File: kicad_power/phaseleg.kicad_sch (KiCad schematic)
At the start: 14 parts, among them Q1 NMOS, Q2 NMOS

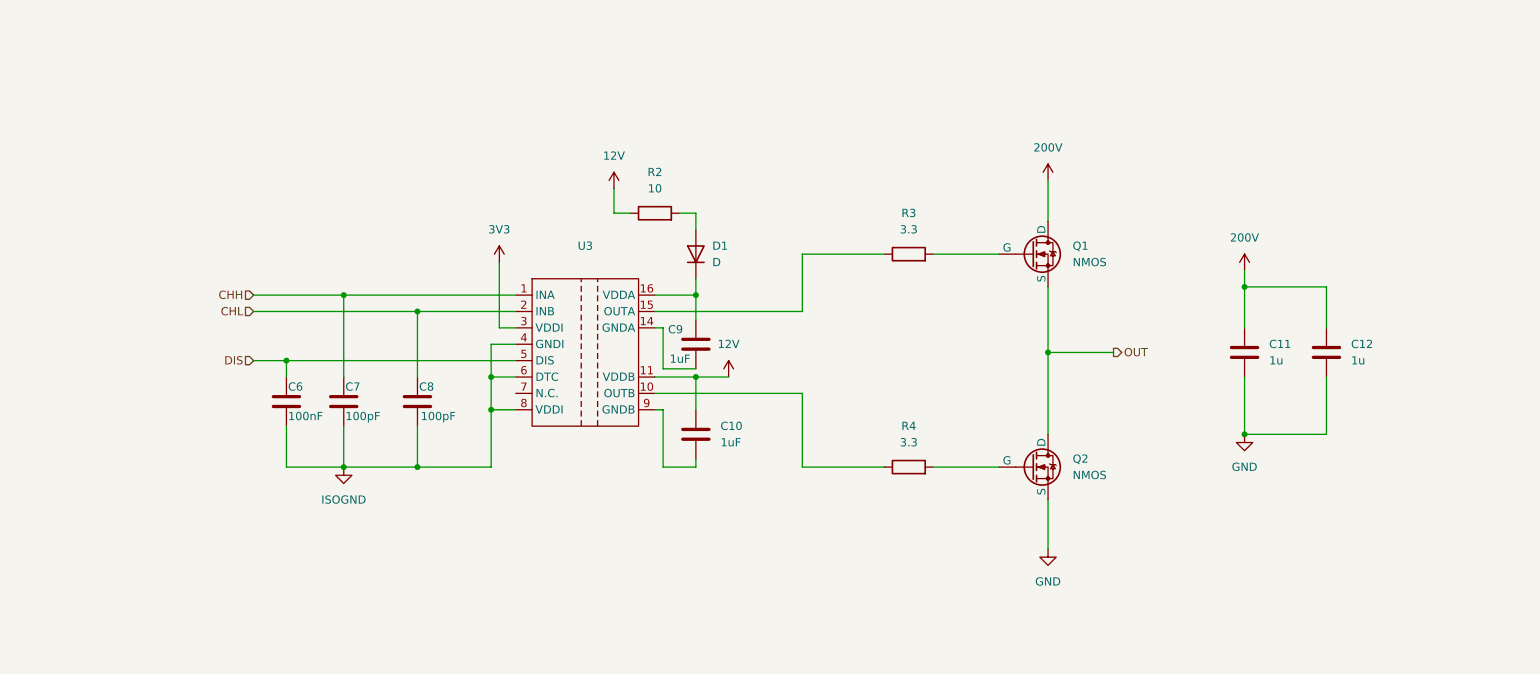
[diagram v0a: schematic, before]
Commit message: finished initial layout of power stage in KiCAD
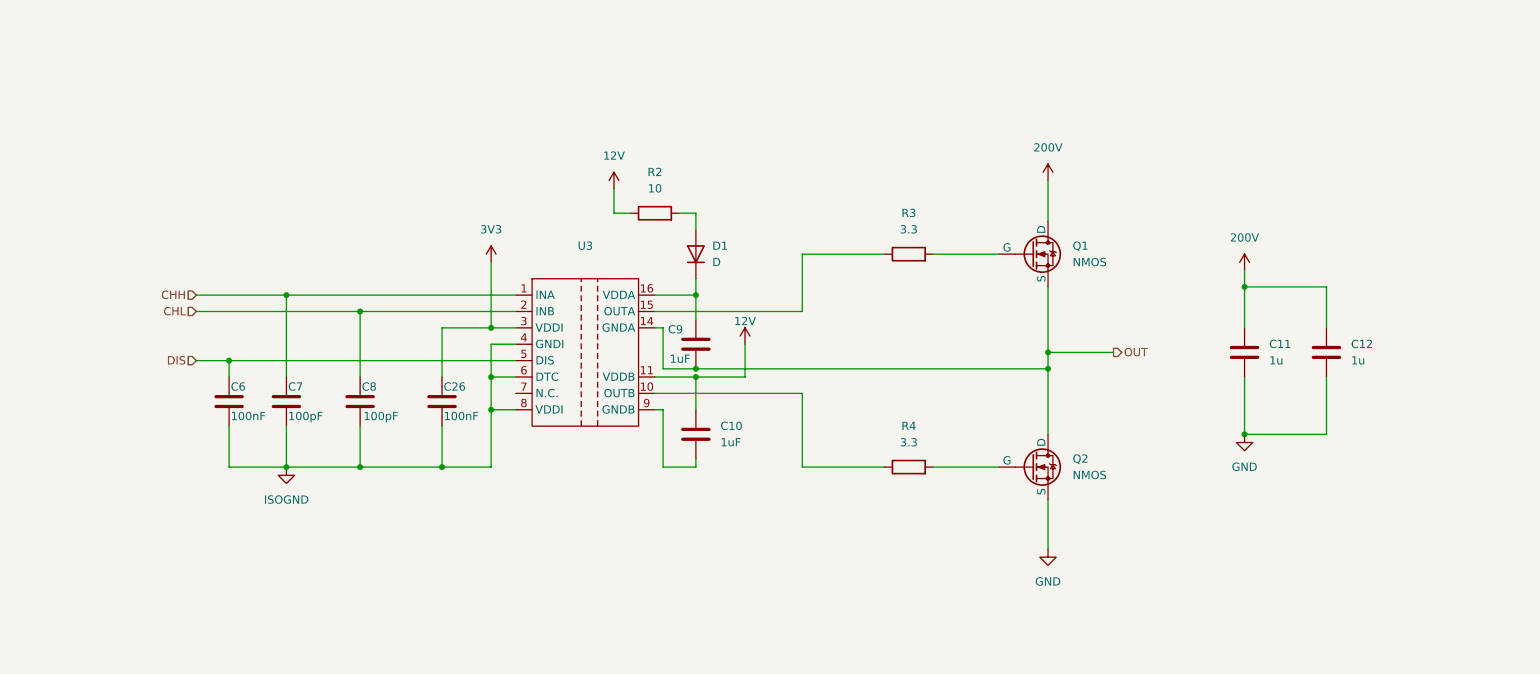
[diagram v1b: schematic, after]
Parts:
- added C26: 100nF, Capacitor_SMD:C_0402_1005Metric, symbol Device:C
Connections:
- net 3V3: now also C26.1
- net ISOGND: now also C26.2
- net OUT: now also C9.2, U3.14 (GNDA)
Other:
- moved on the sheet: C6, C7, C8

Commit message: adjustment to PCB layout, created BOM file, added MOSFET gate discharge diodes
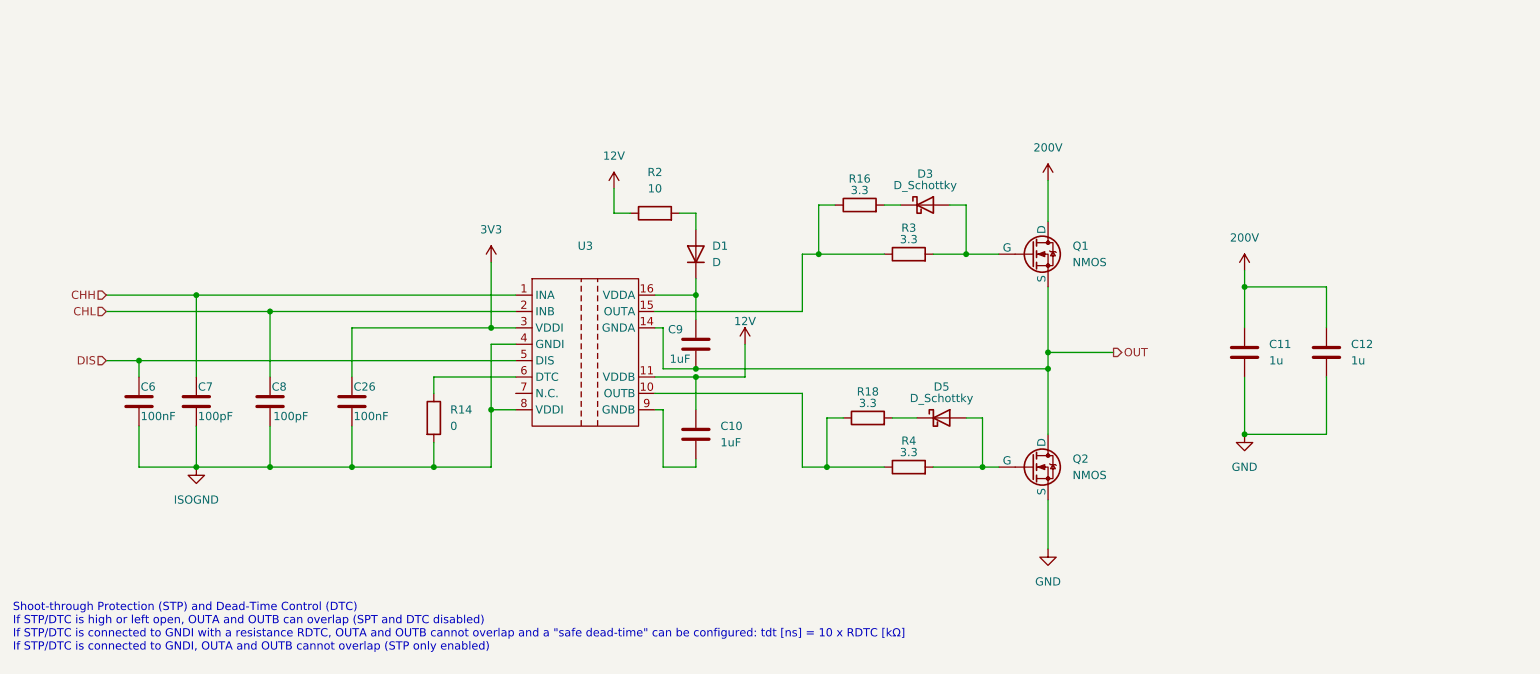
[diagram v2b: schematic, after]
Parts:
- added D3, D5: D_Schottky, Diode_SMD:D_SOD-323F, symbol Device:D_Schottky
- added R14: 0, Resistor_SMD:R_0402_1005Metric, symbol Device:R
- added R16, R18: 3.3, Resistor_SMD:R_0603_1608Metric, symbol Device:R
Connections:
- net ISOGND: now also R14.2; no longer U3.6 (DTC)
- net at Q2.1 (G), R4.2: now also D5.2 (A)
- net at R3.1, U3.15 (OUTA): now also R16.1
- net at Q1.1 (G), R3.2: now also D3.2 (A)
- net at R4.1, U3.10 (OUTB): now also R18.1
- new net: D5.1 (K), R18.2
- new net: R14.1, U3.6 (DTC)
- new net: D3.1 (K), R16.2
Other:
- note added: "Shoot-through Protection (STP) and Dead-Time Control (DTC) If STP/DTC is high or left open, OUTA and OUTB can overlap (SPT and DTC disabled) If STP/DTC is connected to GNDI with a resistance RDTC, OUTA and OUTB cannot overlap and a "safe dead-time" can be configured: tdt [ns] = 10 x RDTC [kΩ] If STP/DTC is connected to GNDI, OUTA and OUTB cannot overlap (STP only enabled)"
- moved on the sheet: C26, C6, C7, C8

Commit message: introduced AGND and A3V3, ensures HV design rules
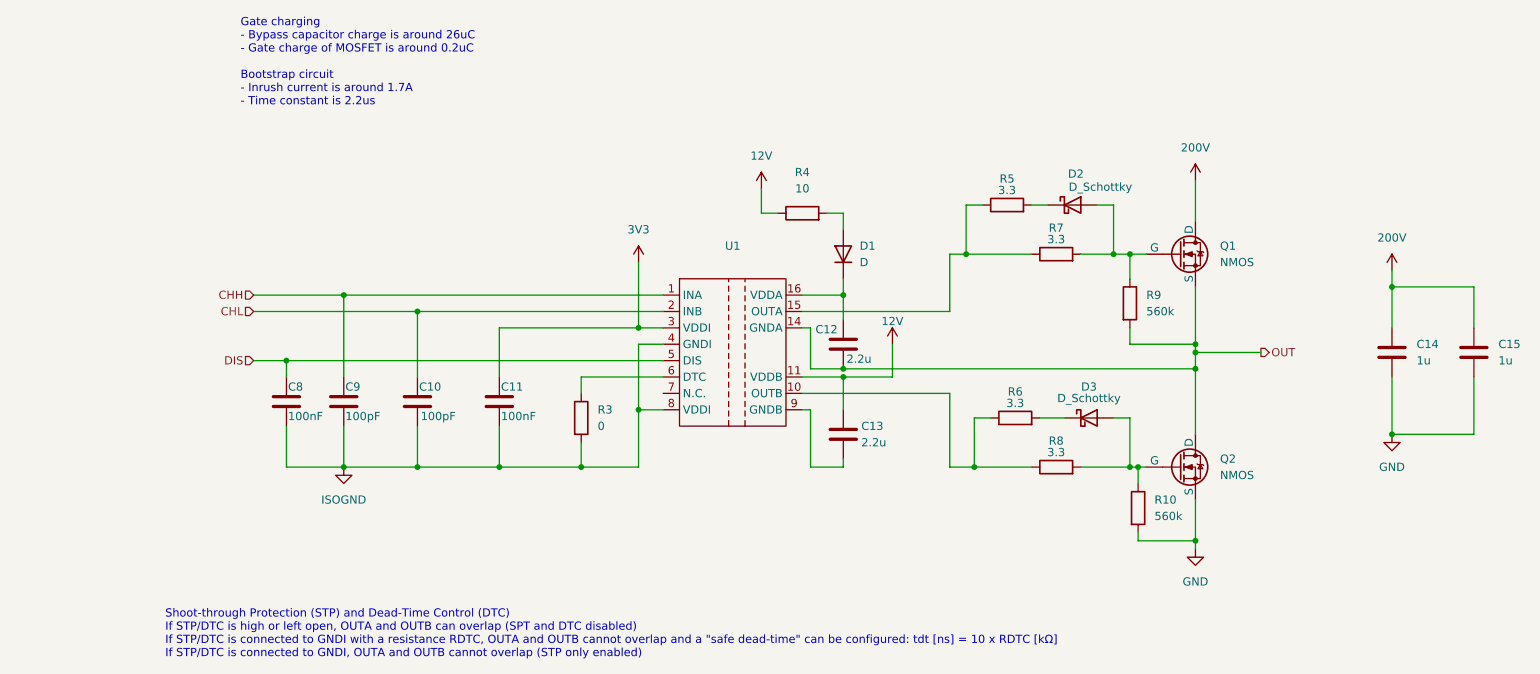
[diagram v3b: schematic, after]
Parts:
- added R10, R9: 560k, Resistor_SMD:R_0402_1005Metric, symbol Device:R
- C12: renamed from C9; value 1uF -> 2.2u; Partno C0603C105K3RACTU -> CGA3E1X7S1C225K080AE
- C13: renamed from C10; value 1uF -> 2.2u; Partno C0603C105K3RACTU -> CGA3E1X7S1C225K080AE
- D1: footprint Diode_SMD:D_SMA -> Diode_SMD:D_SOD-123F; Partno MURA160T3G -> ES1JFL
- Q1, Q2: now left out of the parts list
- renumbered C8 to C10, C26 to C11, C11 to C14, C12 to C15, C6 to C8, C7 to C9, D3 to D2, D5 to D3, R14 to R3, R2 to R4, R16 to R5, R18 to R6, R3 to R7, R4 to R8, U3 to U1
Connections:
- net GND: now also R10.2
- net OUT: now also R9.2
- net at D3.2 (A), Q2.1 (G), R8.2: now also R10.1
- net at D2.2 (A), Q1.1 (G), R7.2: now also R9.1
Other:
- note added: "Gate charging - Bypass capacitor charge is around 26uC - Gate charge of MOSFET is around 0.2uC Bootstrap circuit - Inrush current is around 1.7A - Time constant is 2.2us"
- title: (none) -> Half bridge leg
- moved on the sheet: C10, C11, C12, C13, C14, C15, C8, C9, D1, D2, D3, Q1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

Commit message: finished initial version of power PCB
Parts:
- U1: value ~ -> 2EDB8259Y
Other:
- note added: "2EDB8259Y - UVLO of 8V - 14-SOP package"
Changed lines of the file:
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@@
 	(title_block
 		(title "Half bridge leg")
-		(date "2025-08-06")
+		(date "2025-08-07")
+	)
+	(text "2EDB8259Y\n- UVLO of 8V\n- 14-SOP package"
+		(exclude_from_sim no)
+		(at 109.728 71.374 0)
+		(effects
+			(font
+				(size 1.27 1.27)
+			)
+			(justify left)
+		)
 	)
 	(text "Shoot-through Protection (STP) and Dead-Time Control (DTC) \nIf STP/DTC is high or left open, OUTA and OUTB can overlap (SPT and DTC disabled) \nIf STP/DTC is connected to GNDI with a resistance RDTC, OUTA and OUTB cannot overlap and a \"safe dead-time\" can be configured: tdt [ns] = 10 x RDTC [kΩ] \nIf STP/DTC is connected to GNDI, OUTA and OUTB cannot overlap (STP only enabled) "
@@
 			)
 		)
-		(property "Value" "~"
+		(property "Value" "2EDB8259Y"
 			(at 130.175 82.55 0)
 			(effects

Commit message: finished version 1.1 of power board
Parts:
- added C32: 100nF, Capacitor_SMD:C_0402_1005Metric, symbol Device:C
- C10, C9: JLCPCB (none) -> C26409
- C11, C8: JLCPCB (none) -> C1525
- C12, C13: JLCPCB (none) -> CL10A225KA8NNNC
- C14, C15, Q1, Q2, U1: JLCPCB (none) -> -
- D1: JLCPCB (none) -> C719809
- D2, D3: JLCPCB (none) -> C124210
- R10, R9: JLCPCB (none) -> C15785
- R3: JLCPCB (none) -> C17168
- R4: value 10 -> 18; footprint Resistor_SMD:R_0402_1005Metric -> Resistor_SMD:R_1206_3216Metric; Partno RC0402JR-0710RL -> CRGP1206F18R
- R5, R6: value 3.3 -> 0; JLCPCB (none) -> C25165; Partno CRCW06033R30FKEA -> CRCW06030000ZSTB
- R7, R8: value 3.3 -> 12; Partno CRCW06033R30FKEA -> ERJPA3F12R0V
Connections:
- net 3V3: now also U1.8 (VDDI), C32.1
- net GND: now also C13.2, U1.9 (GNDB)
- net ISOGND: now also C32.2; no longer U1.8 (VDDI)
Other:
- moved on the sheet: C11

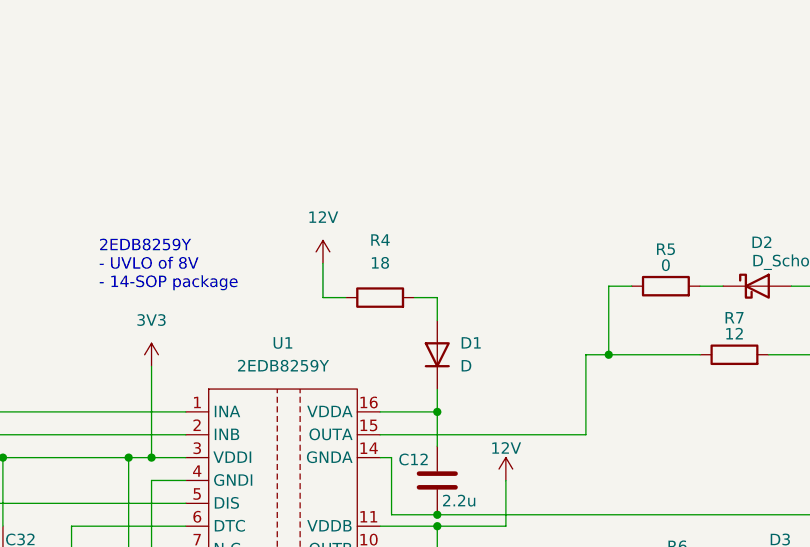
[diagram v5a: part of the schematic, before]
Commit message: replaced bootstrap resistor with anti-surge resistor
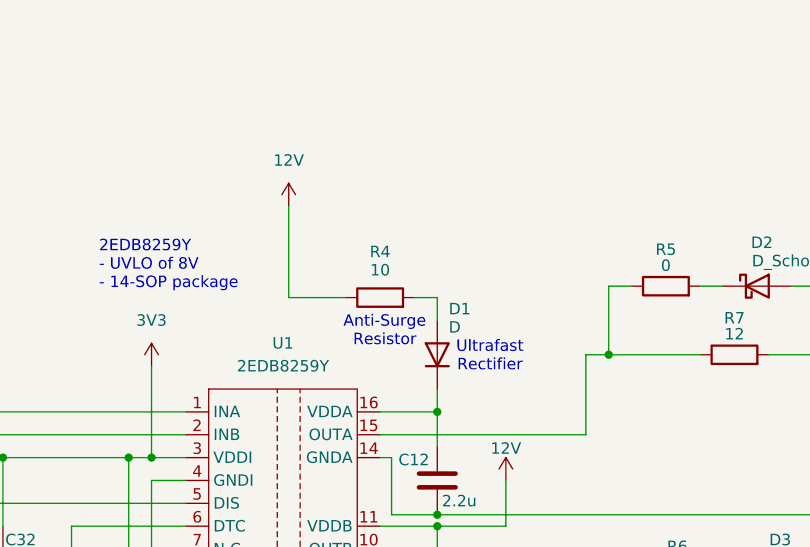
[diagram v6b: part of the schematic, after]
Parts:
- D1: Comment (none) -> Ultrafast Switching Diode
- R4: value 18 -> 10; Comment (none) -> Anti Surge Resistor; Partno CRGP1206F18R -> AS12J10R0ET
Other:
- note added: "Anti-Surge Resistor"
- note added: "Ultrafast Rectifier"
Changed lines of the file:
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@@
 		(rev "1.1")
 	)
+	(text "Ultrafast\nRectifier"
+		(exclude_from_sim no)
+		(at 153.162 81.534 0)
+		(effects
+			(font
+				(size 1.27 1.27)
+			)
+		)
+	)
 	(text "2EDB8259Y\n- UVLO of 8V\n- 14-SOP package"
 		(exclude_from_sim no)
@@
 		)
 	)
+	(text "Anti-Surge \nResistor"
+		(exclude_from_sim no)
+		(at 141.478 78.74 0)
+		(effects
+			(font
+				(size 1.27 1.27)
+			)
+		)
+	)
 	(text "Gate charging\n- Bypass capacitor charge is around 26uC\n- Gate charge of MOSFET is around 0.2uC\n\nBootstrap circuit\n- Inrush current is around 1.7A\n- Time constant is 2.2us"
 		(exclude_from_sim no)
@@
 	(wire
 		(pts
-			(xy 134.62 71.12) (xy 134.62 74.93)
+			(xy 130.81 64.77) (xy 130.81 74.93)
 		)
 		(stroke
@@
 	(wire
 		(pts
-			(xy 134.62 74.93) (xy 137.16 74.93)
+			(xy 130.81 74.93) (xy 137.16 74.93)
 		)
 		(stroke
@@
 		(on_board yes)
 		(dnp no)
-		(fields_autoplaced yes)
 		(property "Reference" "R4"
-			(at 140.97 68.58 90)
+			(at 140.97 69.85 90)
 			(effects
 				(font
@@
 			)
 		)
-		(property "Value" "18"
-			(at 140.97 71.12 90)
+		(property "Value" "10"
+			(at 140.97 71.882 90)
 			(effects
 				(font
@@
 			)
 		)
-		(property "Datasheet" "https://octopart.com/crgp1206f18r-te+connectivity-91018856"
+		(property "Datasheet" "https://octopart.com/as12j10r0et-ohmite-65849002"
 			(at 140.97 74.93 0)
 			(effects
@@
 			)
 		)
-		(property "Description" "Res Thick Film 1206 18 Ohm 1% 0.5W(1/2W) ±100ppm/C Pad SMD Automotive T/R"
+		(property "Description" "Thick Film Resistors - SMD 500mW 10 OHM 5% ANTI SURGE"
 			(at 140.97 74.93 0)
 			(effects
@@
 			)
 		)
-		(property "Partno" "CRGP1206F18R"
+		(property "Partno" "AS12J10R0ET"
 			(at 140.97 74.93 0)
 			(effects
@@
 			)
 		)
+		(property "Comment" "Anti Surge Resistor"
+			(at 140.97 72.136 90)
+			(effects
+				(font
+					(size 1.27 1.27)
+				)
+				(hide yes)
+			)
+		)
 		(pin "2"
 		)
@@
 		(on_board yes)
 		(dnp no)
-		(fields_autoplaced yes)
 		(property "Reference" "D1"
-			(at 149.86 80.0099 90)
+			(at 148.59 76.2 90)
 			(effects
 				(font
@@
 		)
 		(property "Value" "D"
-			(at 149.86 82.5499 90)
+			(at 148.59 78.232 90)
 			(effects
 				(font
@@
 			)
 		)
+		(property "Comment" "Ultrafast Switching Diode"
+			(at 147.828 77.978 90)
+			(effects
+				(font
+					(size 1.27 1.27)
+				)
+				(hide yes)
+			)
+		)
 		(pin "1"
 		)
@@
 	(symbol
 		(lib_id "power:VDD")
-		(at 134.62 71.12 0)
+		(at 130.81 64.77 0)
 		(unit 1)
 		(exclude_from_sim no)
@@
 		(fields_autoplaced yes)
 		(property "Reference" "#PWR015"
-			(at 134.62 74.93 0)
+			(at 130.81 68.58 0)
 			(effects
 				(font
@@
 		)
 		(property "Value" "12V"
-			(at 134.62 66.04 0)
+			(at 130.81 59.69 0)
 			(effects
 				(font
@@
 		)
 		(property "Footprint" ""
-			(at 134.62 71.12 0)
+			(at 130.81 64.77 0)
 			(effects
 				(font
@@
 		)
 		(property "Datasheet" ""
-			(at 134.62 71.12 0)
+			(at 130.81 64.77 0)
 			(effects
 				(font
@@
 		)
 		(property "Description" "Power symbol creates a global label with name \"VDD\""
-			(at 134.62 71.12 0)
+			(at 130.81 64.77 0)
 			(effects
 				(font
